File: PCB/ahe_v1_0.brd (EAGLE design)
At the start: 68.2 x 76.2 mm, 41 parts, among them CN3 1X4-3.5MM, CN4 1X4-3.5MM, IC1 MS560702BA03-50, IC2 MCP73871-1CCI_ML, IC3 ESP32-S2-WROOM-I_M22S2H3200UH3, J1 USB3075-30-A, Q1 TSM200N03DPQ33_RGG

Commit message: fixed schematic bugs in v1_0
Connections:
- new net SPI_SCK: IC3.30
- net EMATCH_1: now also IC3.33; no longer IC3.27
- net EMATCH_2: now also IC3.34; no longer IC3.28
- net IO_1: now also IC3.12
- net IO_2: now also IC3.13
- net IO_3: now also IC3.14
- net IO_4: now also IC3.15
- net SOUND: now also IC3.32; no longer IC3.29
- net SPI_CS: now also IC3.28
- net SPI_MISO: now also IC3.31
- net SPI_MOSI: now also IC3.29
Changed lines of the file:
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@@
 <signal name="SPI_CS">
 <contactref element="JP2" pad="2"/>
+<contactref element="IC3" pad="28"/>
+<wire x1="19.05" y1="10.16" x2="63.36" y2="52.405" width="0" layer="19" extent="1-1"/>
 </signal>
 <signal name="SPI_MOSI">
 <contactref element="JP2" pad="4"/>
+<contactref element="IC3" pad="29"/>
+<wire x1="21.59" y1="10.16" x2="63.36" y2="53.905" width="0" layer="19" extent="1-1"/>
 </signal>
 <signal name="SPI_MISO">
 <contactref element="JP2" pad="6"/>
+<contactref element="IC3" pad="31"/>
+<wire x1="24.13" y1="10.16" x2="63.36" y2="56.905" width="0" layer="19" extent="1-1"/>
 </signal>
 <signal name="SPI_SCLK">
@@
 <signal name="IO_1">
 <contactref element="JP2" pad="11"/>
+<contactref element="IC3" pad="12"/>
+<wire x1="31.75" y1="7.62" x2="45.86" y2="56.905" width="0" layer="19" extent="1-1"/>
 </signal>
 <signal name="IO_2">
 <contactref element="JP2" pad="13"/>
+<contactref element="IC3" pad="13"/>
+<wire x1="34.29" y1="7.62" x2="45.86" y2="55.405" width="0" layer="19" extent="1-1"/>
 </signal>
 <signal name="IO_3">
 <contactref element="JP2" pad="12"/>
+<contactref element="IC3" pad="14"/>
+<wire x1="31.75" y1="10.16" x2="45.86" y2="53.905" width="0" layer="19" extent="1-1"/>
 </signal>
 <signal name="IO_4">
 <contactref element="JP2" pad="14"/>
+<contactref element="IC3" pad="15"/>
+<wire x1="34.29" y1="10.16" x2="45.86" y2="52.405" width="0" layer="19" extent="1-1"/>
 </signal>
 <signal name="N$14">
@@
 </signal>
 <signal name="EMATCH_1">
-<contactref element="IC3" pad="27"/>
 <contactref element="Q1" pad="2"/>
 <wire x1="12.63015" y1="23.7744" x2="12.3825" y2="23.7744" width="0.1778" layer="1"/>
@@
 <wire x1="63.3984" y1="50.8508" x2="66.04" y2="48.2092" width="0.1778" layer="1"/>
 <wire x1="12.3825" y1="23.7744" x2="12.358" y2="23.805" width="0.1778" layer="1"/>
-<wire x1="63.3984" y1="50.8508" x2="63.36" y2="50.905" width="0.1778" layer="1"/>
+<contactref element="IC3" pad="33"/>
+<wire x1="63.3984" y1="50.8508" x2="63.36" y2="59.905" width="0" layer="19" extent="1-1"/>
 </signal>
 <signal name="EMATCH_2">
-<contactref element="IC3" pad="28"/>
 <contactref element="Q1" pad="4"/>
 <wire x1="12.3825" y1="46.31055" x2="12.3825" y2="25.17775" width="0.1778" layer="1"/>
@@
 <wire x1="63.31585" y1="52.41925" x2="61.9125" y2="52.41925" width="0.1778" layer="1"/>
 <wire x1="12.3825" y1="25.17775" x2="12.358" y2="25.105" width="0.1778" layer="1"/>
-<wire x1="63.31585" y1="52.41925" x2="63.36" y2="52.405" width="0.1778" layer="1"/>
+<contactref element="IC3" pad="34"/>
+<wire x1="63.31585" y1="52.41925" x2="63.36" y2="61.405" width="0" layer="19" extent="1-1"/>
 </signal>
 <signal name="SOUND">
-<contactref element="IC3" pad="29"/>
 <contactref element="LS1" pad="1"/>
 <wire x1="63.5635" y1="53.8226" x2="63.3984" y2="53.8226" width="0.1778" layer="1"/>
@@
 <wire x1="62.82055" y1="23.85695" x2="60.83935" y2="25.83815" width="0.1778" layer="16"/>
 <wire x1="62.82055" y1="23.52675" x2="62.82055" y2="23.85695" width="0.1778" layer="16"/>
-<wire x1="63.3984" y1="53.8226" x2="63.36" y2="53.905" width="0.1778" layer="1"/>
 <wire x1="62.82055" y1="23.52675" x2="62.865" y2="23.495" width="0.1778" layer="16"/>
 <via x="60.83935" y="42.5958" extent="1-16" drill="0.35"/>
+<contactref element="IC3" pad="32"/>
+<wire x1="63.3984" y1="53.8226" x2="63.36" y2="58.405" width="0" layer="19" extent="1-1"/>
 </signal>
 <signal name="EMATCH_N+" class="1">
@@
 <wire x1="4.4577" y1="12.46505" x2="4.445" y2="12.545" width="0.254" layer="1"/>
 </signal>
+<signal name="SPI_SCK">
+<contactref element="IC3" pad="30"/>
+</signal>
 </signals>

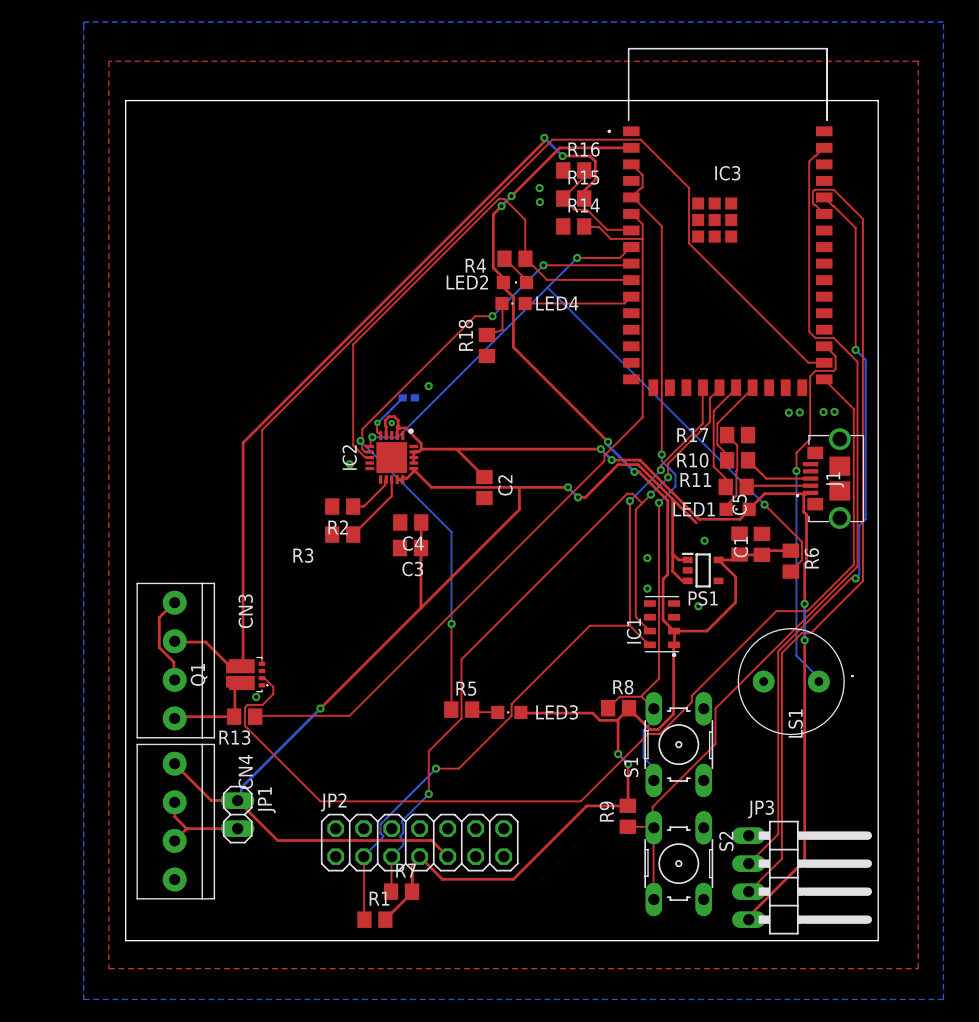
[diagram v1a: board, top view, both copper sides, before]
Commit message: Final schematic and board for ESP32-S2
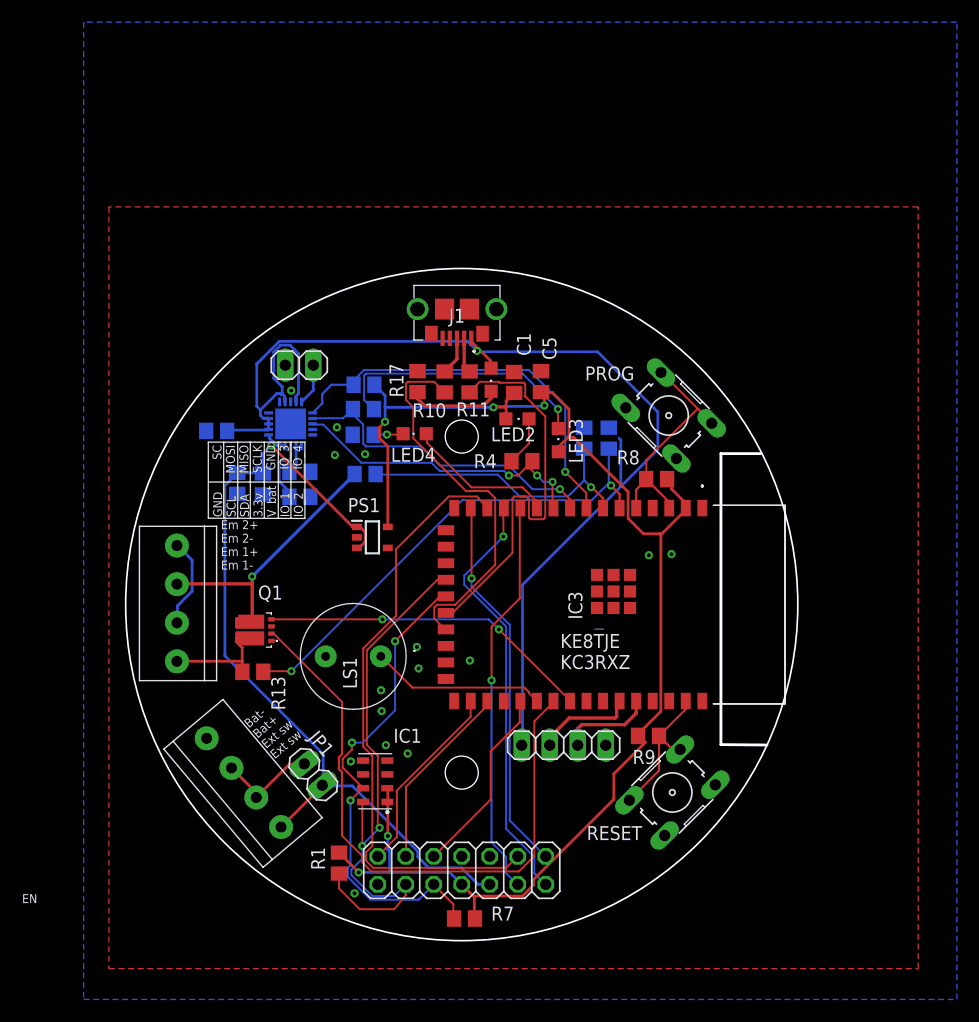
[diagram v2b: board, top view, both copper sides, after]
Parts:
- removed JP3: (no value), pinhead:1X04/90
- removed RT1: 103KT1005T-1P, 103KT1005T-1P:THRMC1005X60N
- added JP4: (no value), pinhead:1X02
- added JP5: (no value), pinhead:1X04
- moved R6 41.9 mm to (21.6, 50.4), flipped to the bottom, turned to 180 degrees
- moved LS1 39.8 mm to (23.1, 25.8)
- moved J1 38.0 mm to (30.0, 57.3), turned to 180 degrees
- moved IC3 36.4 mm to (44.3, 30.5), turned to 270 degrees
- moved R15 31.3 mm to (21.7, 42.3), flipped to the bottom
- moved PS1 30.1 mm to (22.4, 36.6)
- moved S1 29.9 mm to (49.3, 47.6), turned to 315 degrees
- moved IC1 29.7 mm to (22.6, 14.5)
- moved R17 29.4 mm to (26.5, 50.7), turned to 270 degrees
- moved R5 28.7 mm to (21.6, 48.2), flipped to the bottom, turned to 180 degrees
- moved R10 27.5 mm to (28.9, 50.7), turned to 90 degrees
- moved C1 26.8 mm to (35.2, 50.6)
- moved R11 26.0 mm to (31.2, 50.7), turned to 90 degrees
- moved LED1 25.3 mm to (33.1, 50.9), turned to 180 degrees
- moved LED3 25.1 mm to (39.2, 45.4), turned to 0 degrees
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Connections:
- removed net N$9: IC3.41, R9.1, S2.3, S2.4
- new net N$24: IC3.41, R9.1, S2.1, S2.2
- net GND: now also JP4.1, JP5.1, S2.3, S2.4; no longer JP3.1, RT1.1, S2.1, S2.2
- net N$3: now also JP4.2; no longer RT1.2
- net SERIAL_ESP_RX: now also JP5.2; no longer JP3.2
- net SERIAL_ESP_TX: now also JP5.3; no longer JP3.3
- net VCC: now also JP5.4; no longer JP3.4
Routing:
- net N$9: track 81.7 -> 0.00 mm
- net SERIAL_ESP_TX: track 74.0 -> 9.07 mm
- net EMATCH_2: track 94.4 -> 30.2 mm, vias 0 -> 2
- net SERIAL_ESP_RX: track 66.7 -> 8.49 mm, vias 2 -> 0
- net IO_3: track 0.00 -> 55.3 mm
- net EMATCH_2-: track 76.2 -> 26.2 mm, vias 2 -> 1
- net N$10: track 64.6 -> 21.4 mm, vias 2 -> 0
- net V_BAT: track 118.0 -> 78.3 mm, vias 3 -> 1
- net IO_2: track 0.00 -> 38.7 mm, vias 0 -> 1
- net IO_1: track 0.00 -> 36.2 mm, vias 0 -> 1
- net EMATCH_1: track 91.9 -> 55.8 mm
- net IO_4: track 0.00 -> 34.4 mm, vias 0 -> 1
- net BMS_C: track 61.2 -> 29.3 mm, vias 4 -> 1
- net BMS_G: track 67.3 -> 36.6 mm, vias 3 -> 1
- net I2C_SDA: track 72.8 -> 44.7 mm
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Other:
- board size 68.2 x 76.2 mm -> 61 x 61 mm
- board text added: "Astraeus v1.1"
- board text added: "Bat- Bat+ Ext sw Ext sw"
- board text added: "EN"
- board text added: "Em 2+ Em 2- Em 1+ Em 1-"
- board text added: "GND SCL SDA 3.3v V_bat IO_1 IO_2"
- board text added: "KE8TJE KC3RXZ"
- board text added: "PROG"
- board text added: "RESET"
- board text added: "SC MOSI MISO SCLK GND IO_3 IO_4"
- board text added: "WVUER Jan - 2023"
